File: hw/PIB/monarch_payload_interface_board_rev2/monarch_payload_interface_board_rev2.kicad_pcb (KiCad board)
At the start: 4 copper layers, 96 x 89.9 mm, 187 parts, among them J1 5037630291, J10 5037630491, J11 5037630691, J12 5037630691, J13 5037630491, J14 5037630491, J15 5037630691, J16 20021121-00008C4LF, J2 5037630291, J3 5037630691, J4 5037630691, J5 5037630691, J6 5037630691, J7 5037630691, J8 5037630691, J9 5037630491, Q1 FZT600TA, Q10 FZT600TA, Q11 FZT600TA, Q12 FZT600TA, Q13 FZT600TA, Q14 FZT600TA, Q15 FZT600TA, Q16 FZT600TA, Q17 FZT600TA, Q18 FZT600TA, Q19 FZT600TA, Q2 FZT600TA, Q3 FZT600TA, Q4 FZT600TA, Q5 FZT600TA, Q6 FZT600TA, Q7 FZT600TA, Q8 FZT600TA, Q9 FZT600TA, U1 Payload, U10 AD7124-8BCPZ-RL, U11 WSK06121L000FEA, U12 WSK06121L000FEA, U13 WSK06121L000FEA, U14 WSK06121L000FEA, U2 STM32L4A6VGTx, U3 MAX31856MUD_T, U4 TPS61088QRHLRQ1, U5 MAX31856MUD_T, U6 MAX31856MUD_T, U7 MAX31856MUD_T, U8 MAX31856MUD_T, U9 AD7124-8BCPZ-RL

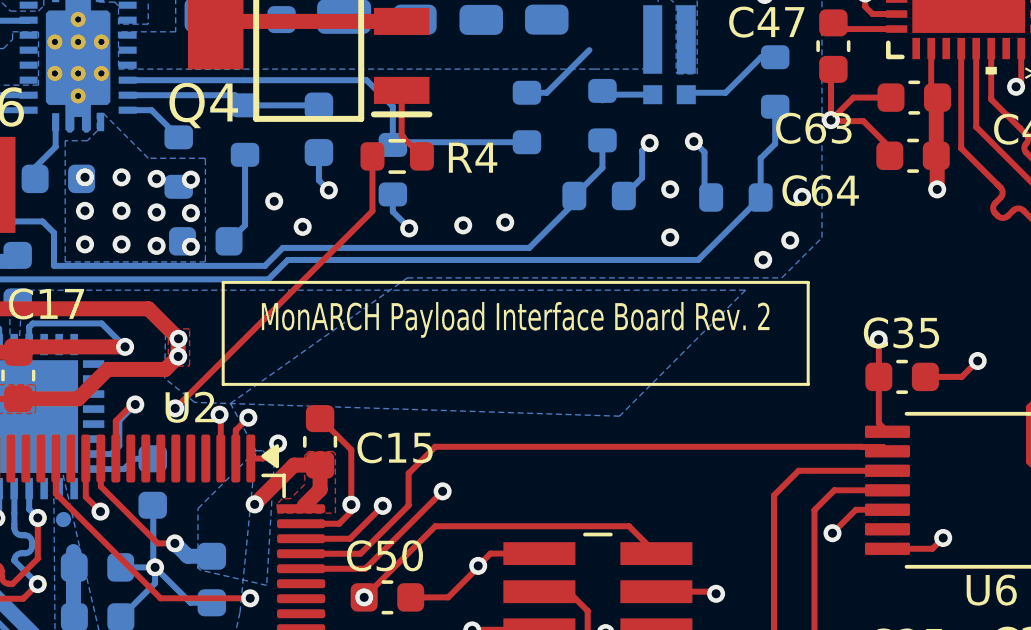
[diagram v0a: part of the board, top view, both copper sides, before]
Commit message: Schematic Clean Up + New Micro-Lock Plus Connectors
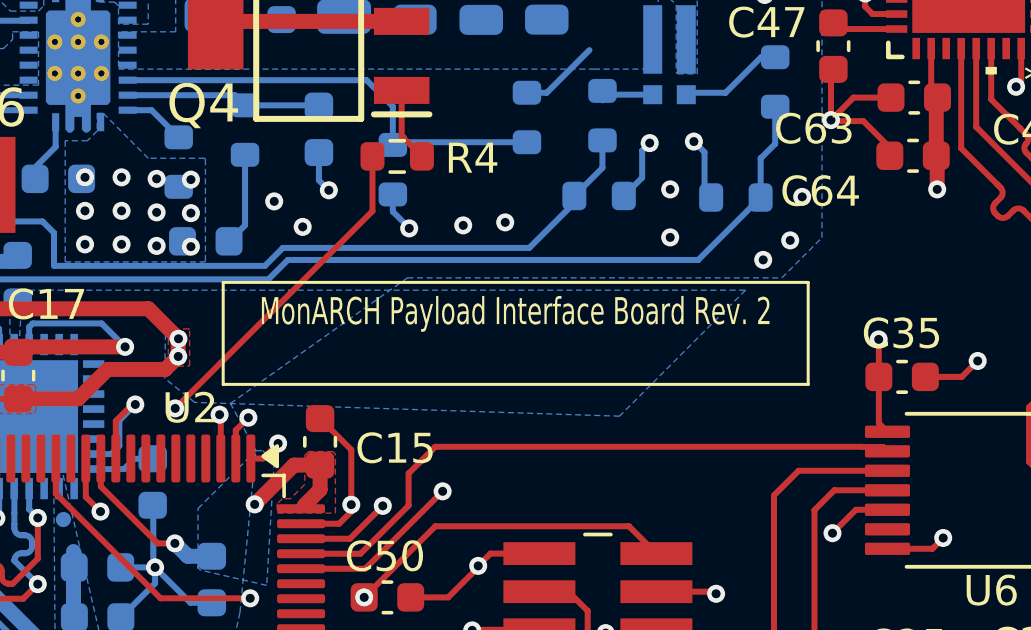
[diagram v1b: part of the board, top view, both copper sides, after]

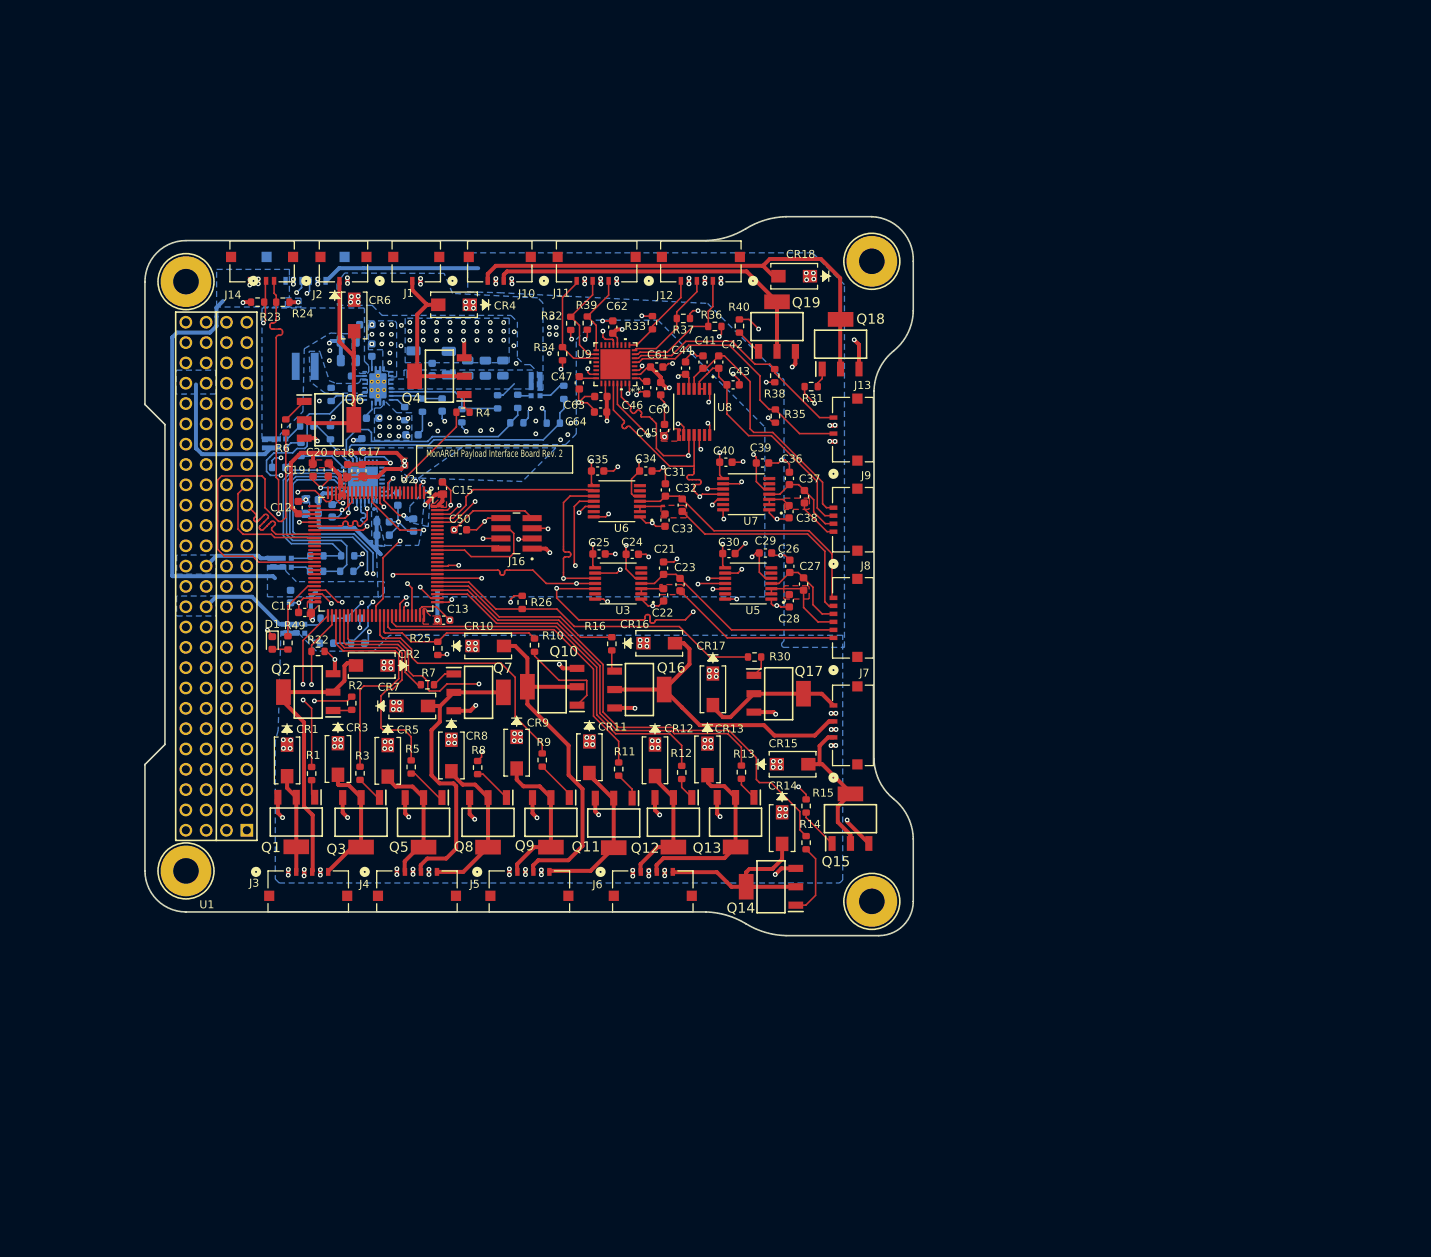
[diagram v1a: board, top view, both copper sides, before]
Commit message: More layout routing (ad7124 pressure routing done)
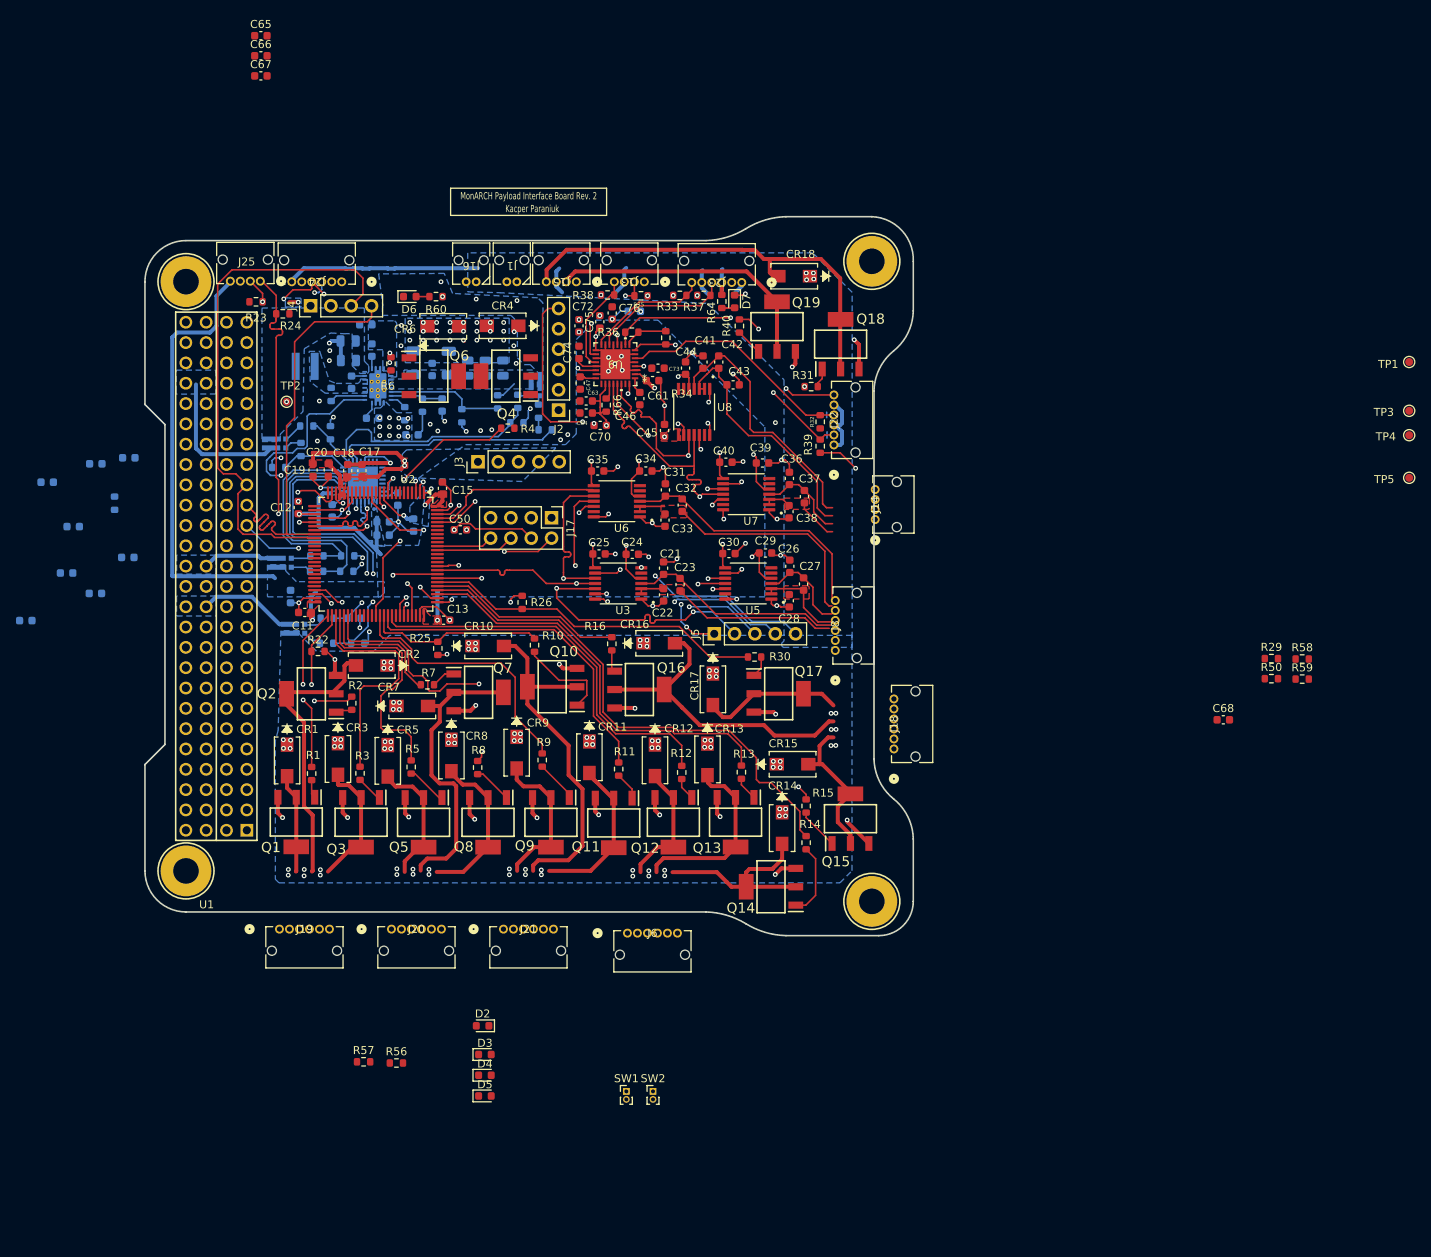
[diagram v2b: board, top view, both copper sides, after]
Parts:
- removed C57, C59, C62: 0.1u, Capacitor_SMD:C_0603_1608Metric
- removed C58, C60: 1u, Capacitor_SMD:C_0603_1608Metric
- removed D1: LED, LED_SMD:LED_0603_1608Metric
- removed J10, J9: 5037630491, 5037630491:CONN_5037630000-SD_04_MOL
- removed J11, J12, J7: 5037630691, 5037630691:CONN_5037630000-SD_06_MOL
- removed R49: 125, Resistor_SMD:R_0603_1608Metric
- added C65: 100n, Capacitor_SMD:C_0603_1608Metric, F.Cu at (48.8, -4.26)
- added C66: 1u, Capacitor_SMD:C_0603_1608Metric, F.Cu at (48.8, -1.75)
- added C67: 100n, Capacitor_SMD:C_0603_1608Metric, F.Cu at (48.8, 0.76)
- added C68: 4.7u, Capacitor_SMD:C_0603_1608Metric, F.Cu at (169.1, 81.2)
- added C69: 0.1u, Capacitor_SMD:C_0603_1608Metric, B.Cu at (32.3, 48.5)
- added C70: 0.1u, Capacitor_SMD:C_0603_1608Metric, F.Cu at (91.2, 44.5)
- added C71: 0.1u, Capacitor_SMD:C_0603_1608Metric, B.Cu at (95.5, 30.2)
- added C72: 0.1u, Capacitor_SMD:C_0603_1608Metric, F.Cu at (88.5, 32.0)
- added C73: 0.1u, Capacitor_SMD:C_0603_1608Metric, F.Cu at (98.4, 37.3)
- added C74: 0.1u, Capacitor_SMD:C_0603_1608Metric, F.Cu at (88.5, 35.3)
- added C75: 1u, Capacitor_SMD:C_0603_1608Metric, F.Cu at (91.2, 31.5)
- added C76: 0.1u, Capacitor_SMD:C_0603_1608Metric, F.Cu at (92.7, 30.4)
- added C87: 1u, Capacitor_SMD:C_0603_1608Metric, B.Cu at (28.1, 49.2)
- added C88: 0.1u, Capacitor_SMD:C_0603_1608Metric, B.Cu at (25.3, 57.1)
- added C89: 0.1u, Capacitor_SMD:C_0603_1608Metric, B.Cu at (22.1, 51.5)
- added C90: 0.1u, Capacitor_SMD:C_0603_1608Metric, B.Cu at (28.1, 65.5)
- added C91: 0.1u, Capacitor_SMD:C_0603_1608Metric, B.Cu at (19.4, 68.8)
- added C92: 0.1u, Capacitor_SMD:C_0603_1608Metric, B.Cu at (24.5, 62.9)
- added C93: 0.1u, Capacitor_SMD:C_0603_1608Metric, B.Cu at (32.1, 61.0)
- added D2: LED, LED_SMD:LED_0603_1608Metric, F.Cu at (76.5, 119.5)
- added D3: LED, LED_SMD:LED_0603_1608Metric, F.Cu at (76.8, 123.1)
- added D4: LED, LED_SMD:LED_0603_1608Metric, F.Cu at (76.8, 125.7)
- added D5: LED, LED_SMD:LED_0603_1608Metric, F.Cu at (76.8, 128.3)
- added D6: LED, LED_SMD:LED_0603_1608Metric, F.Cu at (67.4, 28.4)
- added D7: LED, LED_SMD:LED_0603_1608Metric, F.Cu at (108.0, 29.0)
- added J17: Conn_02x04_Counter_Clockwise, Connector_PinHeader_2.54mm:PinHeader_2x04_P2.54mm_Vertical, F.Cu at (85.1, 56.0)
- added J18: 2200980671, Connector_Molex_Micro-Lock-Plus:Molex_Micro-Lock_2200980671_1x06_P1.25mm_Horizontal, F.Cu at (127.9, 84.9)
- added J19: 2200980671, Connector_Molex_Micro-Lock-Plus:Molex_Micro-Lock_2200980671_1x06_P1.25mm_Horizontal, F.Cu at (51.1, 107.4)
- added J20: 2200980671, Connector_Molex_Micro-Lock-Plus:Molex_Micro-Lock_2200980671_1x06_P1.25mm_Horizontal, F.Cu at (65.1, 107.4)
- added J21: 2200980671, Connector_Molex_Micro-Lock-Plus:Molex_Micro-Lock_2200980671_1x06_P1.25mm_Horizontal, F.Cu at (79.1, 107.4)
- added J22: 2200980671, Connector_Molex_Micro-Lock-Plus:Molex_Micro-Lock_2200980671_1x06_P1.25mm_Horizontal, F.Cu at (120.4, 46.9)
- added J23: 2200980671, Connector_Molex_Micro-Lock-Plus:Molex_Micro-Lock_2200980671_1x06_P1.25mm_Horizontal, F.Cu at (108.9, 26.6)
- added J24: 2200980671, Connector_Molex_Micro-Lock-Plus:Molex_Micro-Lock_2200980671_1x06_P1.25mm_Horizontal, F.Cu at (58.9, 26.5)
- added J25: 2200980471, Connector_Molex_Micro-Lock-Plus:Molex_Micro-Lock_2200980471_1x04_P1.25mm_Horizontal, F.Cu at (48.7, 26.4)
- added R29: 10k, Resistor_SMD:R_0603_1608Metric, F.Cu at (175.1, 73.6)
- added R50: 10k, Resistor_SMD:R_0603_1608Metric, F.Cu at (175.1, 76.1)
- added R56: 125, Resistor_SMD:R_0603_1608Metric, F.Cu at (65.7, 124.2)
- added R57: 125, Resistor_SMD:R_0603_1608Metric, F.Cu at (61.6, 124.0)
- added R58: 125, Resistor_SMD:R_0603_1608Metric, F.Cu at (178.9, 73.7)
- added R59: 125, Resistor_SMD:R_0603_1608Metric, F.Cu at (178.9, 76.2)
- added R60: 1000, Resistor_SMD:R_0603_1608Metric, F.Cu at (70.7, 28.4)
- added R64: 1000, Resistor_SMD:R_0603_1608Metric, F.Cu at (106.4, 29.0)
- added R65: 10k, Resistor_SMD:R_0603_1608Metric, B.Cu at (30.5, 54.2)
- added R66: 10k, Resistor_SMD:R_0603_1608Metric, F.Cu at (91.9, 41.9)
- added SW1: SW_BOOT, Connector_PinHeader_1.00mm:PinHeader_1x02_P1.00mm_Vertical, F.Cu at (94.5, 127.7)
- added SW2: SW_RESET, Connector_PinHeader_1.00mm:PinHeader_1x02_P1.00mm_Vertical, F.Cu at (97.8, 127.7)
- added TP1: TestPoint, TestPoint:TestPoint_Pad_D1.0mm, F.Cu at (192.3, 36.5)
- added TP2: TestPoint, TestPoint:TestPoint_Pad_D1.0mm, F.Cu at (52.0, 41.5)
- added TP3: TestPoint, TestPoint:TestPoint_Pad_D1.0mm, F.Cu at (192.3, 42.6)
- added TP4: TestPoint, TestPoint:TestPoint_Pad_D1.0mm, F.Cu at (192.3, 45.7)
- added TP5: TestPoint, TestPoint:TestPoint_Pad_D1.0mm, F.Cu at (192.3, 51.0)
- J1: value 5037630291 -> 2200980271; footprint 5037630291:CONN_5037630000-SD_02_MOL -> Connector_Molex_Micro-Lock-Plus:Molex_Micro-Lock_2200980271_1x02_P1.25mm_Horizontal
- J13, J14: value 5037630491 -> 2200980471; footprint 5037630491:CONN_5037630000-SD_04_MOL -> Connector_Molex_Micro-Lock-Plus:Molex_Micro-Lock_2200980471_1x04_P1.25mm_Horizontal
- J15: value 5037630691 -> 2200980471; footprint 5037630691:CONN_5037630000-SD_06_MOL -> Connector_Molex_Micro-Lock-Plus:Molex_Micro-Lock_2200980471_1x04_P1.25mm_Horizontal; moved to F.Cu
- J16: value 20021121-00008C4LF -> 2200980271; footprint 20021121:AMPHENOL_20021121-00008C4LF -> Connector_Molex_Micro-Lock-Plus:Molex_Micro-Lock_2200980271_1x02_P1.25mm_Horizontal
- J2: value 5037630291 -> Conn_01x06; footprint 5037630291:CONN_5037630000-SD_02_MOL -> Connector_PinHeader_2.54mm:PinHeader_1x06_P2.54mm_Vertical
- J3, J5: value 5037630691 -> Conn_01x05; footprint 5037630691:CONN_5037630000-SD_06_MOL -> Connector_PinHeader_2.54mm:PinHeader_1x05_P2.54mm_Vertical
- J4: value 5037630691 -> Conn_01x04; footprint 5037630691:CONN_5037630000-SD_06_MOL -> Connector_PinHeader_2.54mm:PinHeader_1x04_P2.54mm_Vertical
- J6, J8: value 5037630691 -> 2200980671; footprint 5037630691:CONN_5037630000-SD_06_MOL -> Connector_Molex_Micro-Lock-Plus:Molex_Micro-Lock_2200980671_1x06_P1.25mm_Horizontal
- R32, R33, R34, R35, R36, R37, R38, R39: value 150 -> 125
- U10, U9: footprint AD7124:CP-32-12_ADI-L -> AD7124:CP-32-12_ADI
- moved J14 83.2 mm to (125.6, 56.2), turned to 90 degrees
- moved J4 74.4 mm to (55.0, 29.5), turned to 90 degrees
- moved J3 57.7 mm to (75.9, 49.0), turned to 90 degrees
- moved J5 39.6 mm to (105.5, 70.5), turned to 90 degrees
- moved J15 33.9 mm to (88.2, 26.5)
- moved J16 33.9 mm to (75.1, 24.5), turned to 180 degrees
- moved R32 33.5 mm to (118.7, 44.0)
- moved R39 32.9 mm to (118.7, 47.0)
- moved J2 32.7 mm to (86.0, 42.5), turned to 180 degrees
- moved J13 32.0 mm to (96.7, 26.5), turned to 180 degrees
- moved R38 23.2 mm to (92.1, 28.1), turned to 0 degrees
- moved R35 22.5 mm to (96.3, 28.2), turned to 180 degrees
- moved R6 15.3 mm to (65.0, 36.8)
- moved Q6 14.2 mm to (70.4, 38.3)
- moved R34 13.1 mm to (99.4, 33.5), turned to -90 degrees
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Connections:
- C10 pad 2: GND -> 12VA_VA-
- C11 pad 2: GND -> 12VA_VA-
- C12 pad 2: GND -> 12VA_VA-
- C13 pad 2: GND -> 12VA_VA-
- C14 pad 2: GND -> 12VA_VA-
- C15 pad 2: GND -> 12VA_VA-
- C16 pad 2: GND -> 12VA_VA-
- C17 pad 1: GND -> 12VA_VA-
- C18 pad 1: GND -> 12VA_VA-
- C19 pad 1: GND -> 12VA_VA-
- C2 pad 2: GND -> 12VA_VA-
- C20 pad 1: GND -> 12VA_VA-
- C21 pad 1: GND -> 12VA_VA-
- C22 pad 2: GND -> 12VA_VA-
- C24 pad 1: GND -> 12VA_VA-
- C25 pad 2: GND -> 12VA_VA-
- C26 pad 1: GND -> 12VA_VA-
- C28 pad 2: GND -> 12VA_VA-
- C29 pad 1: GND -> 12VA_VA-
- C3 pad 2: GND -> 12VA_VA-
- C30 pad 2: GND -> 12VA_VA-
- C31 pad 1: GND -> 12VA_VA-
- C33 pad 2: GND -> 12VA_VA-
- C34 pad 1: GND -> 12VA_VA-
- C35 pad 2: GND -> 12VA_VA-
- C36 pad 1: GND -> 12VA_VA-
- C38 pad 2: GND -> 12VA_VA-
- C39 pad 1: GND -> 12VA_VA-
- C4 pad 1: GND -> 12VA_VA-
- C40 pad 2: GND -> 12VA_VA-
- C41 pad 1: GND -> 12VA_VA-
- C43 pad 2: GND -> 12VA_VA-
- C44 pad 1: GND -> 12VA_VA-
- C45 pad 2: GND -> 12VA_VA-
- C46 pad 1: GND -> 12VA_VA-
- C47 pad 1: GND -> 12VA_VA-
- C48 pad 1: GND -> 12VA_VA-
- C49 pad 1: GND -> 12VA_VA-
- C5 pad 2: GND -> 12VA_VA-
- C50 pad 1: GND -> 12VA_VA-
- C51 pad 2: GND -> 12VA_VA-
- C52 pad 2: GND -> 12VA_VA-
- C53 pad 2: GND -> 12VA_VA-
- C54 pad 2: GND -> 12VA_VA-
- C55 pad 1: GND -> 12VA_VA-
- C56 pad 1: GND -> 12VA_VA-
- C6 pad 2: GND -> 12VA_VA-
- C61 pad 1: GND -> 12VA_VA-
- C63 pad 1: GND -> 12VA_VA-
- C64 pad 1: GND -> 12VA_VA-
- C7 pad 1: GND -> 12VA_VA-
- C8 pad 2: GND -> 12VA_VA-
- C9 pad 2: GND -> 12VA_VA-
- J13 pad 2: P6 -> P6REF+
- J13 pad 4: P7 -> P7REF+
- J14 pad 1: /Connectors/I2C4_SDA -> /Connectors/T3-
- J14 pad 2: /Connectors/I2C4_SCL -> /Connectors/T3+
- J14 pad 3: GND -> /Connectors/T4-
- J14 pad 4: +3V3 -> /Connectors/T4+
- J15 pad 1: +3V3 -> +12VA
- J15 pad 2: GND -> /Connectors/Heater0-
- J15 pad 3: /Connectors/UART_PPU_TX -> +12VA
- J15 pad 4: /Connectors/UART_PPU_RX -> /Connectors/Valve18-
- J16 pad 1: +3V3 -> +12VB
- J16 pad 2: NJTRST -> /Connectors/Valve6-
- J2 pad 1: +12VB -> /Connectors/T5
- J2 pad 2: /Connectors/Valve6- -> /Connectors/T4
- J2 pad 3: (no net) -> /Connectors/T3
- J2 pad 4: (no net) -> /Connectors/T2
- J3 pad 1: +12VA -> /Connectors/SPI1_MISO
- J3 pad 2: /Connectors/Valve1- -> /Connectors/SPI1_MOSI
- J3 pad 3: +12VA -> /Connectors/SPI1_SCK
- J3 pad 4: /Connectors/Valve2- -> /Connectors/ADC
- J3 pad 5: +12VA -> /Connectors/*SYNC
- J4 pad 1: +12VA -> /Connectors/UART_PPU_TX
- J4 pad 2: /Connectors/Valve5- -> /Connectors/UART_PPU_RX
- J4 pad 3: +12VA -> /USART3_RX
- J4 pad 4: /Connectors/Valve7- -> /USART3_TX
- J5 pad 1: +12VA -> /Connectors/SPI2_MISO
- J5 pad 2: /Connectors/Valve9- -> /Connectors/SPI2_MOSI
- J5 pad 3: +12VA -> /Connectors/SPI2_SCK
- J5 pad 4: /Connectors/Valve10- -> *FAULT
- J5 pad 5: +12VA -> *DRDY
- Q1 pad 3: GND -> 12VA_VA-
- Q10 pad 3: GND -> 12VA_VA-
- Q11 pad 3: GND -> 12VA_VA-
- Q12 pad 3: GND -> 12VA_VA-
- Q13 pad 3: GND -> 12VA_VA-
- Q14 pad 3: GND -> 12VA_VA-
- Q15 pad 3: GND -> 12VA_VA-
- Q16 pad 3: GND -> 12VA_VA-
- Q17 pad 3: GND -> 12VA_VA-
- Q18 pad 3: GND -> 12VA_VA-
- Q19 pad 3: GND -> 12VA_VA-
- Q2 pad 3: GND -> 12VA_VA-
- Q3 pad 3: GND -> 12VA_VA-
- Q4 pad 3: GND -> 12VA_VA-
- Q5 pad 3: GND -> 12VA_VA-
- Q6 pad 3: GND -> 12VA_VA-
- Q7 pad 3: GND -> 12VA_VA-
- Q8 pad 3: GND -> 12VA_VA-
- Q9 pad 3: GND -> 12VA_VA-
- R19 pad 2: GND -> 12VA_VA-
- R20 pad 1: GND -> 12VA_VA-
- R22 pad 1: GND -> 12VA_VA-
- R25 pad 1: GND -> 12VA_VA-
- R26 pad 1: GND -> 12VA_VA-
- R32 pad 1: GND -> 12VA_VA-
- R32 pad 2: P1 -> P1REF+
- R33 pad 1: GND -> 12VA_VA-
- R33 pad 2: P5 -> P5REF+
- R34 pad 1: GND -> 12VA_VA-
- R34 pad 2: P2 -> P2REF+
- R35 pad 1: GND -> 12VA_VA-
- R35 pad 2: P6 -> P6REF+
- R36 pad 1: GND -> 12VA_VA-
- R36 pad 2: P3 -> P3REF+
- R37 pad 1: GND -> 12VA_VA-
- R37 pad 2: P4 -> P4REF+
- R38 pad 1: GND -> 12VA_VA-
- R38 pad 2: P7 -> P7REF+
- R39 pad 1: GND -> 12VA_VA-
- R39 pad 2: P0 -> P0REF+
- R41 pad 1: GND -> 12VA_VA-
- R41 pad 2: 3V3_VB -> 3V3_VB+
- R42 pad 1: 12VA_VB -> 12VA_VB+
- R43 pad 1: GND -> 12VA_VA-
- R43 pad 2: 12VA_VB -> 12VA_VB+
- R44 pad 1: GND -> 12VA_VA-
- R44 pad 2: 12VA_VA -> 12VA_VA+
- R45 pad 1: 12VA_VA -> 12VA_VA+
- R46 pad 1: GND -> 12VA_VA-
- R46 pad 2: 12VB_VA -> 12VB_VA+
- R47 pad 1: 12VB_VA -> 12VB_VA+
- R48 pad 1: 12VB_VB -> 12VB_VB+
- R51 pad 1: GND -> 12VA_VA-
- R51 pad 2: VBAT_VA -> VBAT_VA+
- R52 pad 1: GND -> 12VA_VA-
- R52 pad 2: VBAT_VB -> VBAT_VB+
- R53 pad 1: VBAT_VA -> VBAT_VA+
- R54 pad 1: VBAT_VB -> VBAT_VB+
- R55 pad 1: GND -> 12VA_VA-
- R55 pad 2: 12VB_VB -> 12VB_VB+
- R61 pad 1: GND -> 12VA_VA-
- R61 pad 2: 3V3_VA -> 3V3_VA+
- R62 pad 1: 3V3_VB -> 3V3_VB+
- R63 pad 1: 3V3_VA -> 3V3_VA+
- U1 pad 100: GND -> 12VA_VA-
- U1 pad 33: /MCU/USART3_TX -> /USART3_TX
- U1 pad 35: /MCU/USART3_RX -> /USART3_RX
- U1 pad 61: GND -> 12VA_VA-
- U1 pad 66: GND -> 12VA_VA-
- U1 pad 69: GND -> 12VA_VA-
- U1 pad 73: GND -> 12VA_VA-
- U1 pad 74: GND -> 12VA_VA-
- U1 pad 81: GND -> 12VA_VA-
- U1 pad 82: GND -> 12VA_VA-
- U1 pad 84: GND -> 12VA_VA-
- U1 pad 99: GND -> 12VA_VA-
- U10 pad 10: 12VB_VA -> VBAT_VA+
- U10 pad 11: 12VB_VB -> 12VA_VA-
- U10 pad 12: +3V3 -> Net-(U10-REFIN1(+))
- U10 pad 13: GND -> 12VA_VA-
- U10 pad 14: unconnected-(U10-AIN8/IOUT/VBIAS-Pad14) -> 3V3_VA+
- U10 pad 15: unconnected-(U10-AIN9/IOUT/VBIAS-Pad15) -> 12VA_VA-
- U10 pad 16: unconnected-(U10-AIN10/IOUT/VBIAS-Pad16) -> 3V3_VB+
- U10 pad 17: unconnected-(U10-AIN11/IOUT/VBIAS-Pad17) -> 12VA_VA-
- U10 pad 18: unconnected-(U10-AIN12/IOUT/VBIAS-Pad18) -> 12VA_VA+
- U10 pad 19: unconnected-(U10-AIN13/IOUT/VBIAS-Pad19) -> 12VA_VA-
- U10 pad 20: unconnected-(U10-AIN14/IOUT/VBIAS/REFIN2(+)-Pad20) -> 12VA_VB+
- U10 pad 21: unconnected-(U10-AIN15/IOUT/VBIAS/REFIN2(-)-Pad21) -> 12VA_VA-
- U10 pad 22: unconnected-(U10-REFOUT-Pad22) -> Net-(U10-REFIN1(+))
- U10 pad 23: GND -> 12VA_VA-
- U10 pad 27: unconnected-(U10-*SYNC-Pad27) -> /PC104 Stack/*SYNC
- U10 pad 28: /MCU/SPI1_MISO -> /Connectors/SPI1_MISO
- U10 pad 29: /MCU/SPI1_MOSI -> /Connectors/SPI1_MOSI
- U10 pad 3: GND -> 12VA_VA-
- U10 pad 30: /MCU/SPI1_SCK -> /Connectors/SPI1_SCK
- U10 pad 32: /MCU/ADC -> /Connectors/ADC
- U10 pad 33: unconnected-(U10-EP-Pad33) -> 12VA_VA-
- U10 pad 4: 12VA_VB -> 12VB_VB+
- U10 pad 5: 12VA_VA -> 12VA_VA-
- U10 pad 6: 3V3_VB -> 12VB_VA+
- U10 pad 7: 3V3_VA -> 12VA_VA-
- U10 pad 8: VBAT_VA -> VBAT_VB+
- U10 pad 9: VBAT_VB -> 12VA_VA-
- U2 pad 1: /MCU/T4 -> /Connectors/T4
- U2 pad 10: GND -> 12VA_VA-
- U2 pad 19: GND -> 12VA_VA-
- U2 pad 2: /MCU/T2 -> /Connectors/T2
- U2 pad 20: GND -> 12VA_VA-
- U2 pad 27: GND -> 12VA_VA-
- U2 pad 29: /MCU/ADC -> /Connectors/ADC
- U2 pad 3: /MCU/PT -> /Connectors/PT
- U2 pad 30: /MCU/SPI1_SCK -> /Connectors/SPI1_SCK
- U2 pad 31: /MCU/SPI1_MISO -> /Connectors/SPI1_MISO
- U2 pad 32: /MCU/SPI1_MOSI -> /Connectors/SPI1_MOSI
- U2 pad 33: /MCU/USART3_TX -> /USART3_TX
- U2 pad 34: /MCU/USART3_RX -> /USART3_RX
- U2 pad 44: unconnected-(U2-PE13-Pad44) -> /MCU/BLUE_LED
- U2 pad 45: unconnected-(U2-PE14-Pad45) -> /MCU/GREEN_LED
- U2 pad 46: Net-(U2-PE15) -> /MCU/RED_LED
- U2 pad 49: GND -> 12VA_VA-
- U2 pad 6: unconnected-(U2-VBAT-Pad6) -> +3V3
- U2 pad 73: unconnected-(U2-VDDUSB-Pad73) -> +3V3
- U2 pad 74: GND -> 12VA_VA-
- U2 pad 82: /MCU/SPI2_SCK -> /Connectors/SPI2_SCK
- U2 pad 84: /MCU/SPI2_MISO -> /Connectors/SPI2_MISO
- U2 pad 85: /MCU/SPI2_MOSI -> /Connectors/SPI2_MOSI
- U2 pad 91: unconnected-(U2-PB5-Pad91) -> /Connectors/*SYNC
- U2 pad 94: unconnected-(U2-PH3-Pad94) -> Net-(U2-PH3)
- U2 pad 96: /MCU/T1 -> /Connectors/T1
- U2 pad 97: /MCU/T3 -> /Connectors/T3
- U2 pad 98: /MCU/T5 -> /Connectors/T5
- U2 pad 99: GND -> 12VA_VA-
- U3 pad 1: GND -> 12VA_VA-
- U3 pad 10: /MCU/SPI2_SCK -> /Connectors/SPI2_SCK
- U3 pad 11: /MCU/SPI2_MISO -> /Connectors/SPI2_MISO
- U3 pad 12: /MCU/SPI2_MOSI -> /Connectors/SPI2_MOSI
- U3 pad 13: unconnected-(U3-~{FAULT}-Pad13) -> *FAULT
- U3 pad 14: GND -> 12VA_VA-
- U3 pad 7: unconnected-(U3-~{DRDY}-Pad7) -> *DRDY
- U3 pad 9: /MCU/T1 -> /Connectors/T1
- U4 pad 11: GND -> 12VA_VA-
- U4 pad 12: GND -> 12VA_VA-
- U4 pad 13: GND -> 12VA_VA-
- U4 pad 20: GND -> 12VA_VA-
- U4 pad 21: GND -> 12VA_VA-
- U5 pad 1: GND -> 12VA_VA-
- U5 pad 10: /MCU/SPI2_SCK -> /Connectors/SPI2_SCK
- U5 pad 11: /MCU/SPI2_MISO -> /Connectors/SPI2_MISO
- U5 pad 12: /MCU/SPI2_MOSI -> /Connectors/SPI2_MOSI
- U5 pad 14: GND -> 12VA_VA-
- U5 pad 9: /MCU/T2 -> /Connectors/T2
- U6 pad 1: GND -> 12VA_VA-
- U6 pad 10: /MCU/SPI2_SCK -> /Connectors/SPI2_SCK
- U6 pad 11: /MCU/SPI2_MISO -> /Connectors/SPI2_MISO
- U6 pad 12: /MCU/SPI2_MOSI -> /Connectors/SPI2_MOSI
- U6 pad 14: GND -> 12VA_VA-
- U6 pad 9: /MCU/T3 -> /Connectors/T3
- U7 pad 1: GND -> 12VA_VA-
- U7 pad 10: /MCU/SPI2_SCK -> /Connectors/SPI2_SCK
- U7 pad 11: /MCU/SPI2_MISO -> /Connectors/SPI2_MISO
- U7 pad 12: /MCU/SPI2_MOSI -> /Connectors/SPI2_MOSI
- U7 pad 14: GND -> 12VA_VA-
- U7 pad 9: /MCU/T4 -> /Connectors/T4
- U8 pad 1: GND -> 12VA_VA-
- U8 pad 10: /MCU/SPI2_SCK -> /Connectors/SPI2_SCK
- U8 pad 11: /MCU/SPI2_MISO -> /Connectors/SPI2_MISO
- U8 pad 12: /MCU/SPI2_MOSI -> /Connectors/SPI2_MOSI
- U8 pad 14: GND -> 12VA_VA-
- U8 pad 9: /MCU/T5 -> /Connectors/T5
- U9 pad 10: unconnected-(U9-AIN6/IOUT/VBIAS-Pad10) -> P3REF+
- U9 pad 11: unconnected-(U9-AIN7/IOUT/VBIAS-Pad11) -> 12VA_VA-
- U9 pad 12: +3V3 -> Net-(U9-REFIN1(+))
- U9 pad 13: GND -> 12VA_VA-
- U9 pad 14: unconnected-(U9-AIN8/IOUT/VBIAS-Pad14) -> P4REF+
- U9 pad 15: unconnected-(U9-AIN9/IOUT/VBIAS-Pad15) -> 12VA_VA-
- U9 pad 16: unconnected-(U9-AIN10/IOUT/VBIAS-Pad16) -> P5REF+
- U9 pad 17: P0 -> 12VA_VA-
- U9 pad 18: P1 -> P6REF+
- U9 pad 19: P2 -> 12VA_VA-
- U9 pad 20: unconnected-(U9-AIN14/IOUT/VBIAS/REFIN2(+)-Pad20) -> P7REF+
- U9 pad 21: unconnected-(U9-AIN15/IOUT/VBIAS/REFIN2(-)-Pad21) -> 12VA_VA-
- U9 pad 22: unconnected-(U9-REFOUT-Pad22) -> Net-(U9-REFIN1(+))
- U9 pad 23: GND -> 12VA_VA-
- U9 pad 27: unconnected-(U9-*SYNC-Pad27) -> Net-(U9-*SYNC)
- U9 pad 28: /MCU/SPI2_MISO -> /Connectors/SPI2_MISO
- U9 pad 29: /MCU/SPI2_MOSI -> /Connectors/SPI2_MOSI
- U9 pad 3: GND -> 12VA_VA-
- U9 pad 30: /MCU/SPI2_SCK -> /Connectors/SPI2_SCK
- U9 pad 32: /MCU/PT -> /Connectors/PT
- U9 pad 33: unconnected-(U9-EP-Pad33) -> 12VA_VA-
- U9 pad 4: unconnected-(U9-AIN0/IOUT/VBIAS-Pad4) -> P0REF+
- U9 pad 5: P6 -> 12VA_VA-
- U9 pad 6: P7 -> P1REF+
- U9 pad 7: P3 -> 12VA_VA-
- U9 pad 8: P4 -> P2REF+
- U9 pad 9: P5 -> 12VA_VA-
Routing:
- net 12VA_VA-: track 0.00 -> 356.2 mm, vias 0 -> 147
- net GND: track 320.9 -> 0.00 mm, vias 156 -> 0
- net (no net): track 0.00 -> 171.7 mm, vias 0 -> 4
- net /Connectors/SPI2_MOSI: track 0.00 -> 119.7 mm, vias 0 -> 8
- net /MCU/SPI2_MOSI: track 113.4 -> 0.00 mm, vias 8 -> 0
- net /Connectors/SPI2_SCK: track 0.00 -> 110.7 mm, vias 0 -> 6
- net /Connectors/SPI2_MISO: track 0.00 -> 107.4 mm, vias 0 -> 6
- net /MCU/SPI2_SCK: track 101.1 -> 0.00 mm, vias 5 -> 0
- net /MCU/SPI2_MISO: track 100.5 -> 0.00 mm, vias 4 -> 0
- net /MCU/T2: track 70.3 -> 0.00 mm, vias 2 -> 0
- net /Connectors/T2: track 0.00 -> 70.3 mm, vias 0 -> 2
- net /USART3_RX: track 0.00 -> 66.9 mm
- net /Connectors/PT: track 0.00 -> 63.1 mm, vias 0 -> 3
- net /MCU/T4: track 55.4 -> 0.00 mm, vias 2 -> 0
- net /Connectors/T4: track 0.00 -> 55.4 mm, vias 0 -> 2
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- added copper zone on B.Cu, net 12VA_VA-
- added copper zone on In1.Cu, net 12VA_VA-
- added copper zone on In2.Cu, net 12VA_VA-
- removed copper zone on B.Cu, net GND
- removed copper zone on In1.Cu, net GND
- removed copper zone on In2.Cu, net GND
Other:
- board text added: "Kacper Paraniuk"

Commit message: Progress
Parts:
- moved C68 141.9 mm to (55.0, -3.17)
- moved R50 124.7 mm to (51.5, 59.8)
- moved R58 123.5 mm to (67.2, 126.2)
- moved R29 114.8 mm to (75.3, 130.4)
- moved TP4 96.3 mm to (145.9, 130.1)
- moved TP1 96.3 mm to (145.9, 120.9)
- moved TP3 96.3 mm to (145.9, 127.0)
- moved TP5 96.3 mm to (145.9, 135.4)
- moved SW2 88.2 mm to (23.6, 80.0), turned to 90 degrees
- moved R59 82.4 mm to (98.4, 58.8), turned to 180 degrees
- moved D5 73.7 mm to (101.5, 58.8), turned to 180 degrees
- moved D2 60.1 mm to (50.3, 65.4), turned to -90 degrees
- moved R57 59.3 mm to (52.1, 65.5), turned to 90 degrees
- moved SW1 22.6 mm to (79.4, 144.5), turned to -90 degrees
- moved C50 10.0 mm to (82.9, 53.4)
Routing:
- net +3V3: track 176.4 -> 195.7 mm, vias 21 -> 20
- net 12VA_VA-: track 356.2 -> 364.8 mm, vias 147 -> 145
- net /MCU/NRST: track 48.4 -> 54.5 mm
- net /USART3_RX: track 66.9 -> 64.8 mm, vias 0 -> 1
- net Net-(D5-A): track 0.00 -> 1.45 mm
- net +12VA: track 50.5 -> 51.8 mm
- net /MCU/RED_LED: track 0.83 -> 0.00 mm
- net /Connectors/UART_PPU_RX: track 44.6 -> 44.1 mm, vias 4 -> 3
- net /Connectors/Valve4-: vias 1 -> 0

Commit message: Layout Rev Done - NO DRC Check
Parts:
- R65: moved to F.Cu
- moved TP3 114.4 mm to (82.7, 31.7)
- moved TP5 105.0 mm to (89.2, 47.1)
- moved SW1 87.1 mm to (74.6, 57.5), turned to 0 degrees
- moved C65 78.4 mm to (68.9, 71.5), turned to 90 degrees
- moved C66 76.4 mm to (70.4, 71.5), turned to 90 degrees
- moved R29 72.3 mm to (72.7, 58.2), turned to 90 degrees
- moved D4 68.0 mm to (49.9, 63.2)
- moved D3 67.0 mm to (49.9, 61.7)
- moved R58 64.6 mm to (52.9, 63.2)
- moved R56 63.7 mm to (52.9, 61.7)
- moved C68 53.4 mm to (65.6, 49.2)
- moved C67 52.7 mm to (65.6, 50.7)
- moved C91 46.7 mm to (60.5, 46.5), turned to 90 degrees
- moved R65 44.2 mm to (74.2, 61.0), turned to 0 degrees
- moved C88 41.1 mm to (66.3, 53.2)
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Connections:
- R29 pad 2: Net-(U2-PH3) -> unconnected-(R29-Pad2)
- R65 pad 1: /PC104 Stack/*SYNC -> /Connectors/*SYNC
- SW1 pad 1: Net-(U2-PH3) -> unconnected-(R29-Pad2)
- U10 pad 10: VBAT_VA+ -> 3V3_VA+
- U10 pad 14: 3V3_VA+ -> VBAT_VA+
- U10 pad 16: 3V3_VB+ -> VBAT_VB+
- U10 pad 18: 12VA_VA+ -> 12VB_VA+
- U10 pad 20: 12VA_VB+ -> 12VB_VB+
- U10 pad 27: /PC104 Stack/*SYNC -> /Connectors/*SYNC
- U10 pad 4: 12VB_VB+ -> 12VA_VB+
- U10 pad 6: 12VB_VA+ -> 12VA_VA+
- U10 pad 8: VBAT_VB+ -> 3V3_VB+
- U2 pad 4: unconnected-(U2-PE5-Pad4) -> /MCU/Valve6
- U2 pad 40: /MCU/Valve6 -> unconnected-(U2-PE9-Pad40)
- U2 pad 94: Net-(U2-PH3) -> unconnected-(R29-Pad2)
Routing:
- net (no net): track 171.7 -> 0.00 mm, vias 4 -> 0
- net 3V3_VA+: track 0.00 -> 48.9 mm
- net /Connectors/*SYNC: track 0.00 -> 42.3 mm, vias 0 -> 4
- net 12VA_VB+: track 0.00 -> 37.8 mm, vias 0 -> 2
- net 12VA_VA+: track 0.01 -> 35.3 mm, vias 0 -> 2
- net 12VA_VA-: track 364.8 -> 398.5 mm, vias 145 -> 123
- net /Connectors/ADC: track 6.18 -> 37.0 mm
- net /Connectors/T1: track 35.4 -> 65.5 mm, vias 2 -> 3
- net 3V3_VB+: track 0.00 -> 28.2 mm
- net /Connectors/SPI1_SCK: track 11.0 -> 37.4 mm
- net /Connectors/Valve6-: track 0.00 -> 25.9 mm
- net 12VB_VB+: track 1.50 -> 24.9 mm
- net 12VB_VA+: track 0.00 -> 22.1 mm
- net /Connectors/Valve4-: track 0.00 -> 21.9 mm
- net /Connectors/SPI1_MOSI: track 11.0 -> 32.9 mm
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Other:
- board text added: "+12VB"
- board text added: "+12Va"
- board text added: "3V3"
- board text added: "GND"
